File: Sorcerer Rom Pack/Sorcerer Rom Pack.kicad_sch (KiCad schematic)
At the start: 88 parts

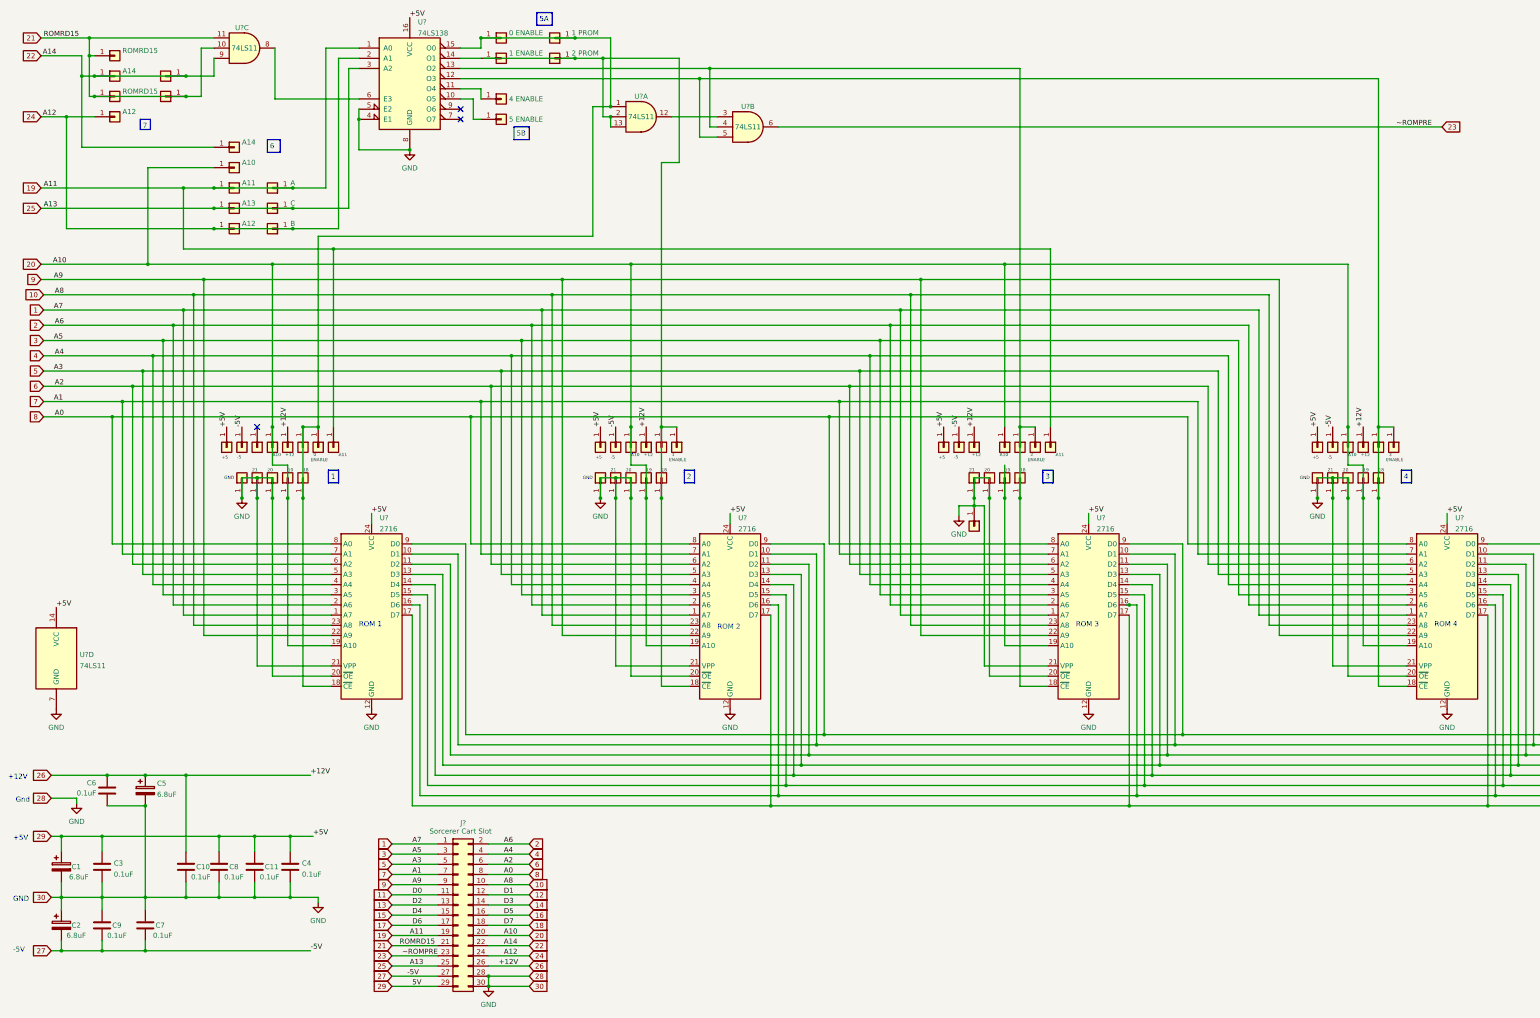
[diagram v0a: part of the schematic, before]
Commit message: added rom pak
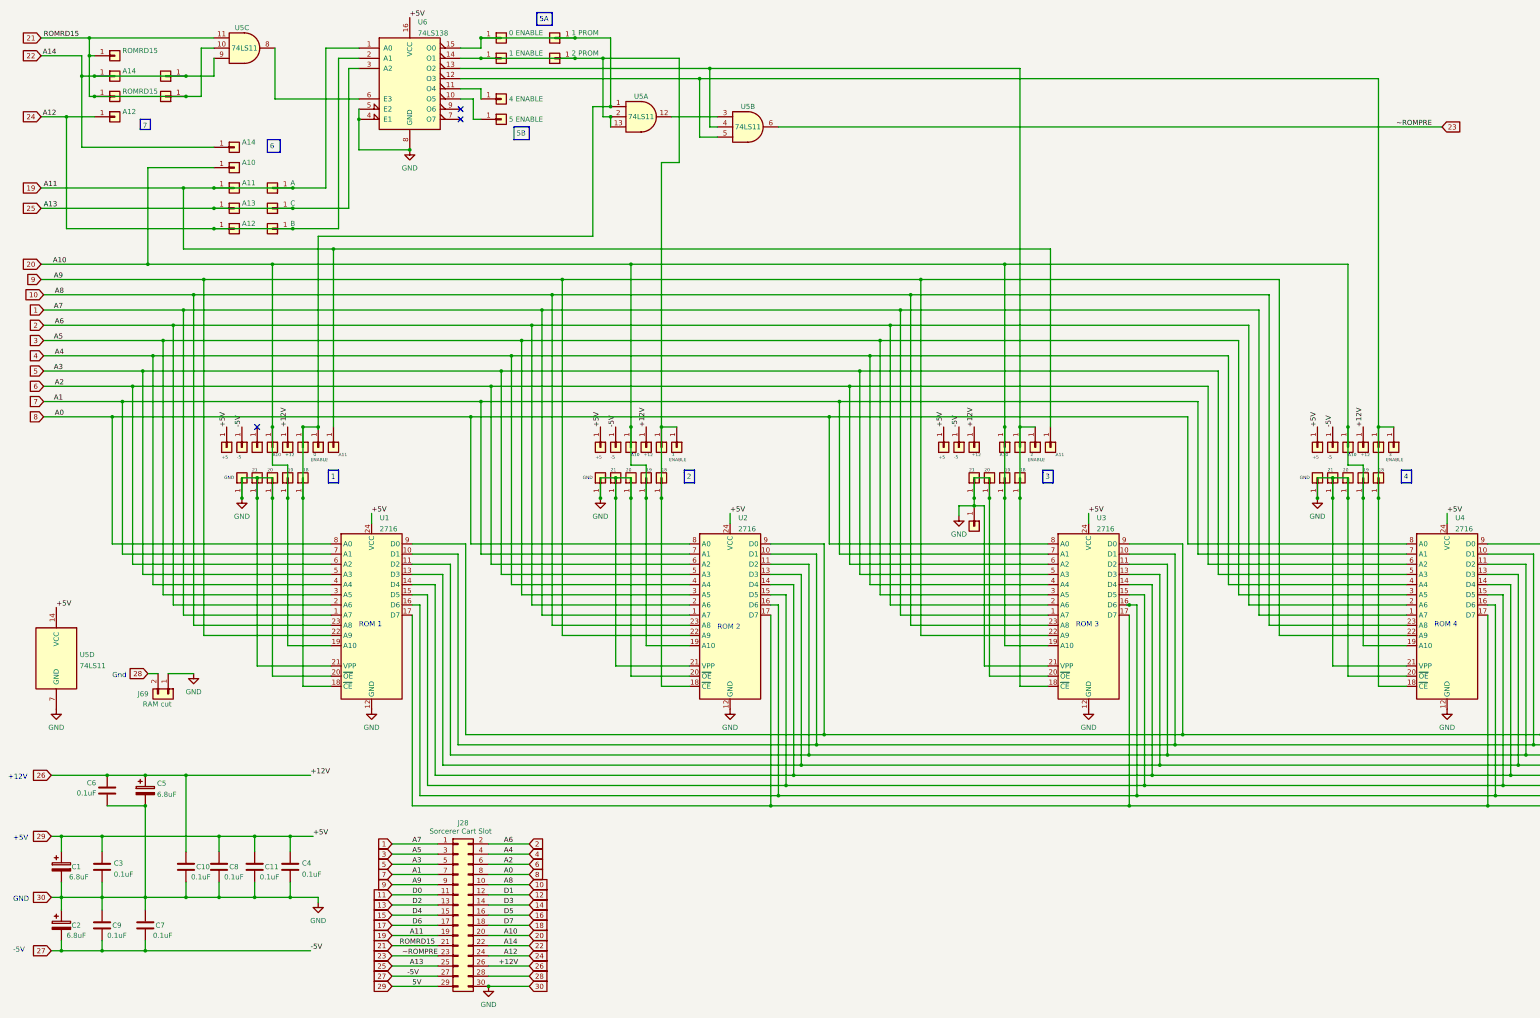
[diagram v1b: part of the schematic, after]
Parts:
- added J69: RAM cut, Jumper:SolderJumper-2_P1.3mm_Open_RoundedPad1.0x1.5mm, symbol Connector_Generic:Conn_01x02
- C1, C2, C5: footprint (none) -> Capacitor_THT:CP_Radial_Tantal_D4.5mm_P5.00mm
- C10, C11, C3, C4, C6, C7, C8, C9: footprint (none) -> Capacitor_THT:C_Disc_D4.3mm_W1.9mm_P5.00mm
- J1, J10, J11, J12, J13, J14, J15, J16, J17, J18, J19, J2, J20, J21, J22, J23, J24, J25, J26, J27, J29, J3, J30, J31, J32, J33, J34, J35, J36, J37, J38, J39, J4, J40, J41, J42, J43, J44, J45, J46, J47, J48, J49, J5, J50, J51, J52, J53, J54, J55, J56, J57, J58, J59, J6, J60, J61, J62, J63, J64, J65, J66, J67, J68, J7, J8, J9: renamed from J?; footprint (none) -> Connector_PinHeader_2.54mm:PinHeader_1x01_P2.54mm_Vertical
- J28: renamed from J?; footprint (none) -> Evan's misc parts:edge mounted 30 pin card edge connector (2x15 pin)
- U5: renamed from U?; footprint (none) -> Package_DIP:DIP-14_W7.62mm
- U6: renamed from U?; footprint (none) -> Package_DIP:DIP-16_W7.62mm
- gave numbers to parts that had none: 4
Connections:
- net 20: now also J53.1 (Pin_1), U3.19 (A10)
- net GND: now also J69.1 (Pin_1); no longer J28.28 (Pin_28)
- net at J30.1 (Pin_1), U6.14 (O1): now also J34.1 (Pin_1), J43.1 (Pin_1), J44.1 (Pin_1), J45.1 (Pin_1), U2.18 (~{CE}), U5.13, U5.2
- new net 28: J28.28 (Pin_28), J69.2 (Pin_2)

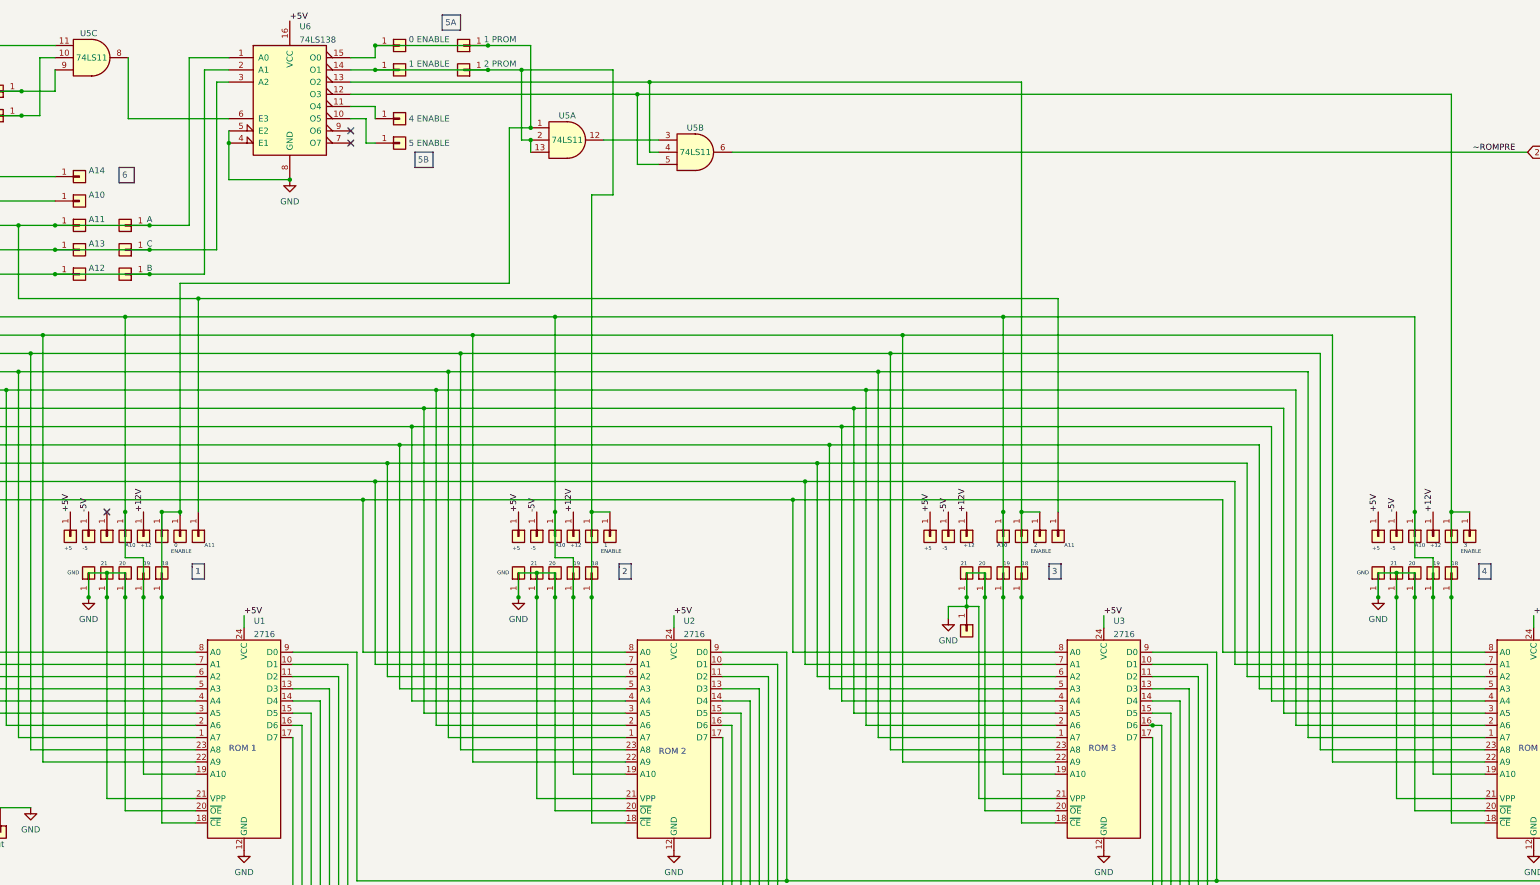
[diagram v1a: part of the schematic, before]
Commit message: many tweaks and experimental silk
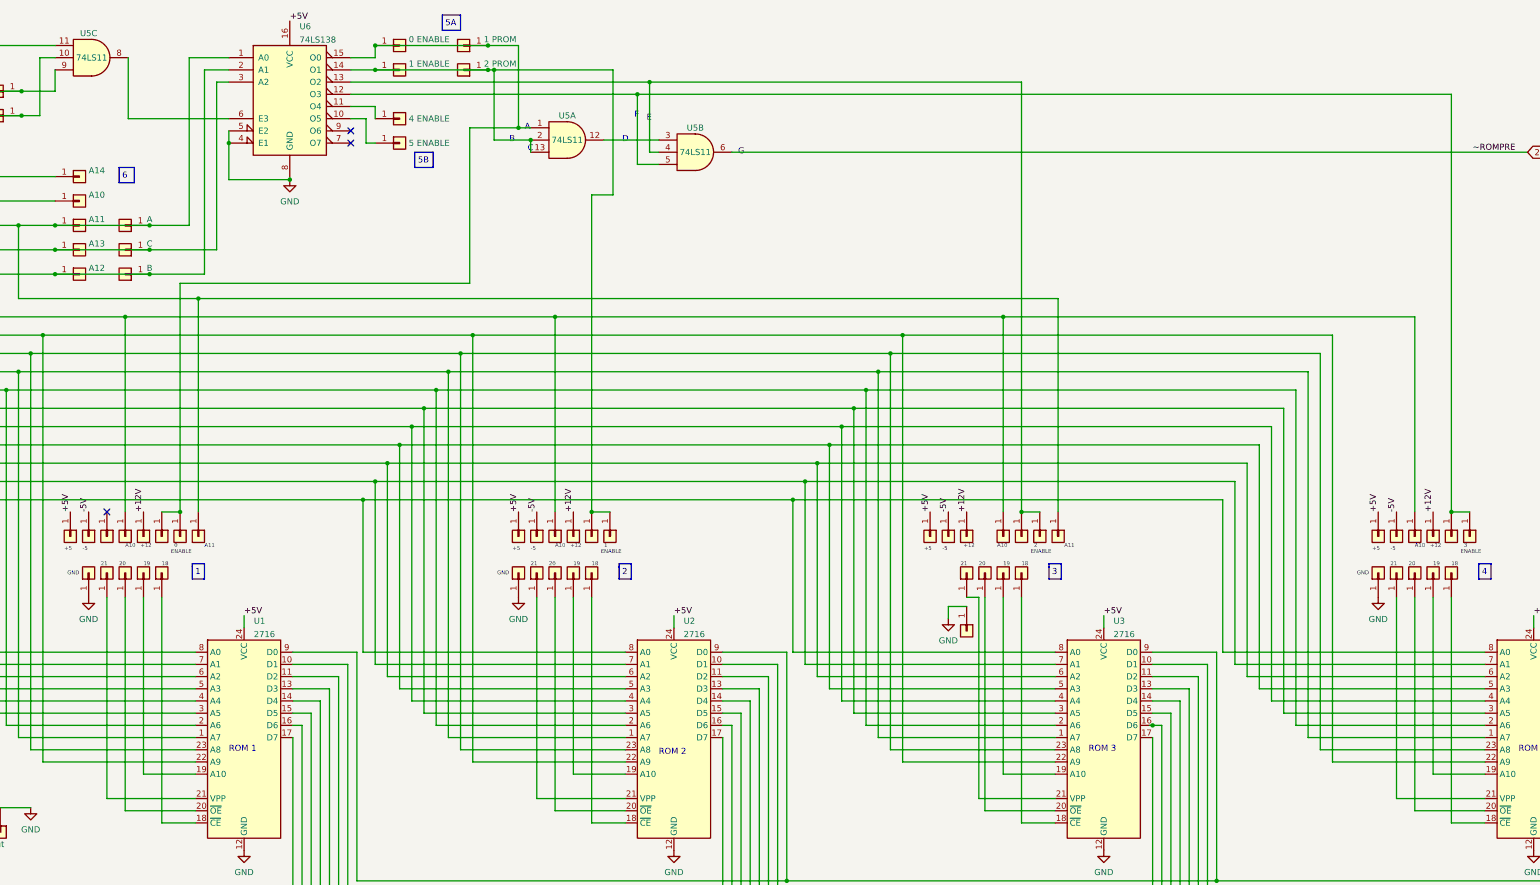
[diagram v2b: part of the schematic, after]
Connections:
- net 20: no longer J23.1 (Pin_1), J42.1 (Pin_1), J53.1 (Pin_1), J65.1 (Pin_1), U1.19 (A10), U2.19 (A10), U3.19 (A10), U4.19 (A10)
- net GND: no longer J16.1 (Pin_1), J21.1 (Pin_1), J38.1 (Pin_1), J40.1 (Pin_1), J49.1 (Pin_1), J51.1 (Pin_1), J61.1 (Pin_1), J63.1 (Pin_1), U1.20 (~{OE}), U1.21 (VPP), U2.20 (~{OE}), U2.21 (VPP), U3.20 (~{OE}), U3.21 (VPP), U4.20 (~{OE}), U4.21 (VPP)
- net at J54.1 (Pin_1), J56.1 (Pin_1), U5.4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: no longer J55.1 (Pin_1), U3.18 (~{CE})
- net at J66.1 (Pin_1), J68.1 (Pin_1), U5.5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: no longer J67.1 (Pin_1), U4.18 (~{CE})
- net at J24.1 (Pin_1), J26.1 (Pin_1), J29.1 (Pin_1)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: no longer J25.1 (Pin_1), U1.18 (~{CE})
- net at J30.1 (Pin_1), J34.1 (Pin_1), J43.1 (Pin_1)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: no longer J44.1 (Pin_1), U2.18 (~{CE})
- new net: J67.1 (Pin_1), U4.18 (~{CE})
- new net: J65.1 (Pin_1), U4.19 (A10)
- new net: J63.1 (Pin_1), U4.20 (~{OE})
- new net: J61.1 (Pin_1), U4.21 (VPP)
- new net: J25.1 (Pin_1), U1.18 (~{CE})
- new net: J23.1 (Pin_1), U1.19 (A10)
- new net: J21.1 (Pin_1), U1.20 (~{OE})
- new net: J16.1 (Pin_1), U1.21 (VPP)
- new net: J53.1 (Pin_1), U3.19 (A10)
- new net: J44.1 (Pin_1), U2.18 (~{CE})
- new net: J42.1 (Pin_1), U2.19 (A10)
- new net: J40.1 (Pin_1), U2.20 (~{OE})
- new net: J38.1 (Pin_1), U2.21 (VPP)
- new net: J55.1 (Pin_1), U3.18 (~{CE})
- new net: J51.1 (Pin_1), U3.20 (~{OE})
- new net: J49.1 (Pin_1), U3.21 (VPP)
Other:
- note added: "A"
- note added: "B"
- note added: "C"
- note added: "D"
- note added: "E"
- note added: "F"
- note added: "G"

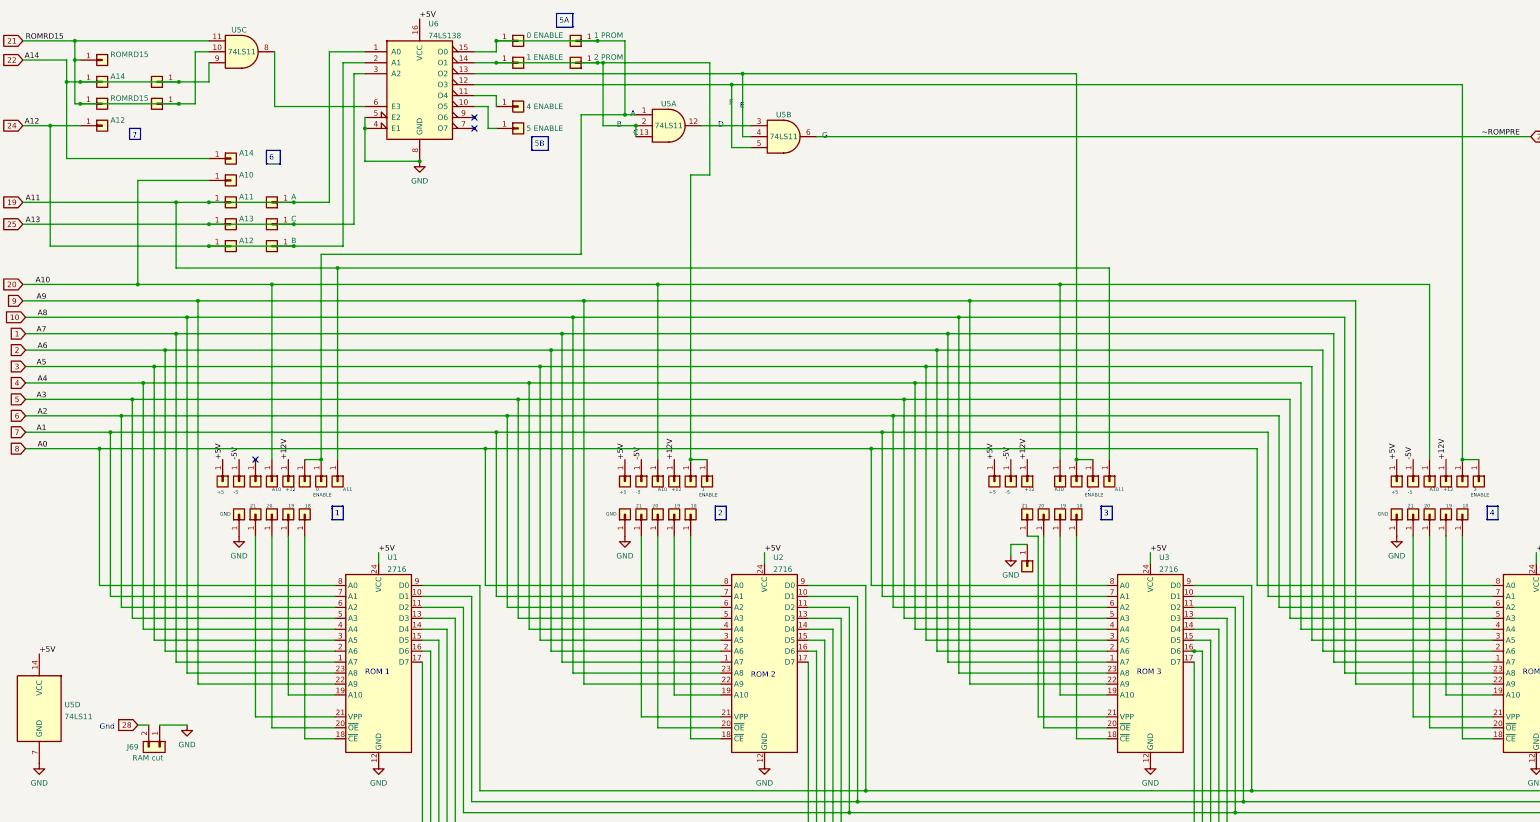
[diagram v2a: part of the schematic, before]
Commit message: removed temp files, added gitignore, fixed silk on rom pac board
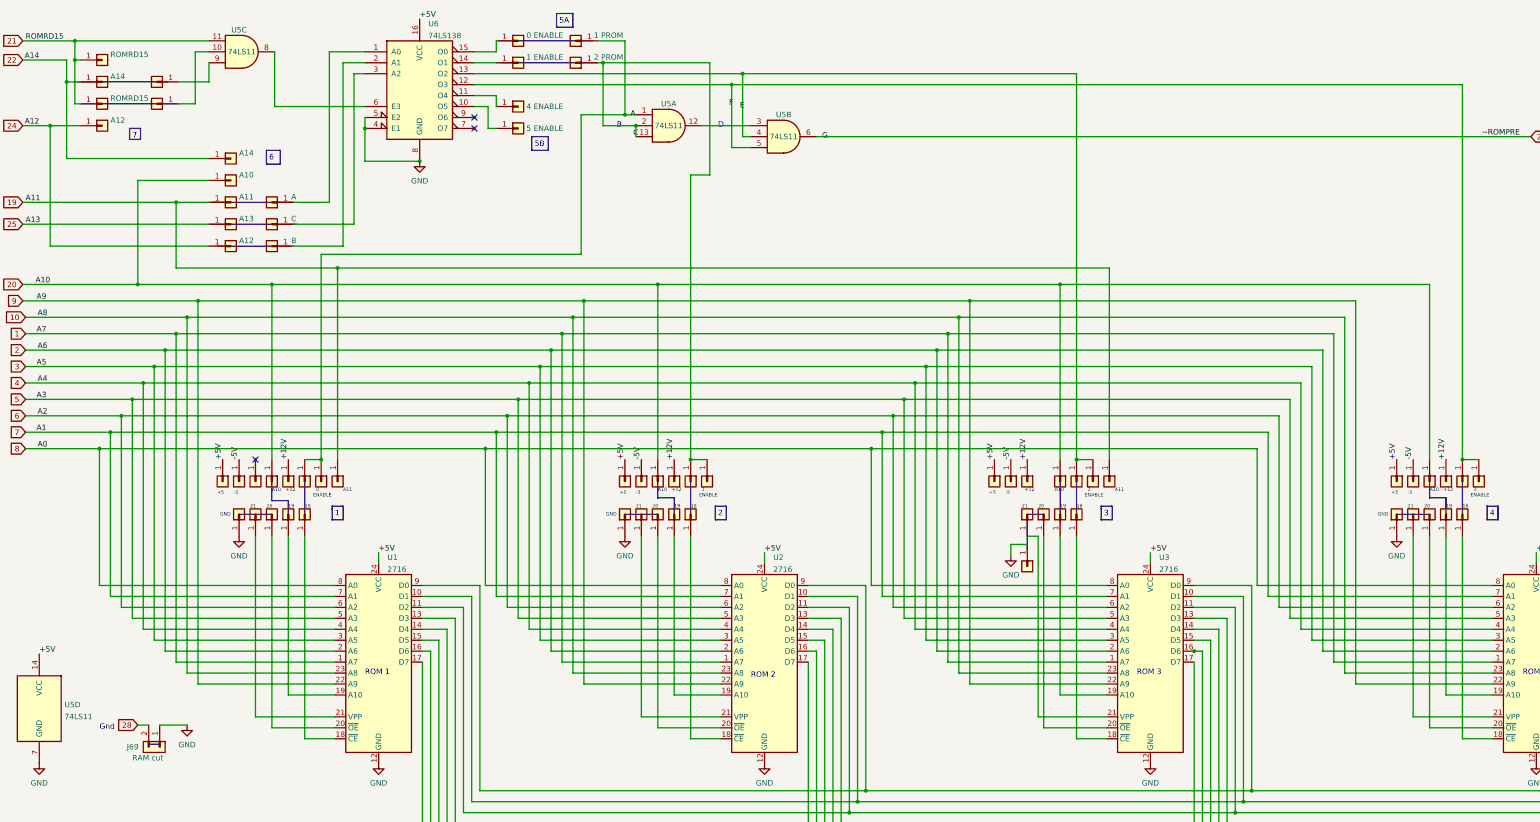
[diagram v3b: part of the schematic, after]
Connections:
- net 19: no longer J17.1 (Pin_1), U6.1 (A0)
- net 21: no longer J6.1 (Pin_1), U5.10
- net 22: no longer J5.1 (Pin_1), U5.9
- net 24: no longer J19.1 (Pin_1), U6.2 (A1)
- net 25: no longer J18.1 (Pin_1), U6.3 (A2)
- net at J34.1 (Pin_1), J43.1 (Pin_1), J45.1 (Pin_1)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: no longer J30.1 (Pin_1), U6.14 (O1)
- net at J24.1 (Pin_1), J26.1 (Pin_1), J33.1 (Pin_1)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: no longer J29.1 (Pin_1), U6.15 (O0)
- new net: J30.1 (Pin_1), U6.14 (O1)
- new net: J29.1 (Pin_1), U6.15 (O0)
- new net: J19.1 (Pin_1), U6.2 (A1)
- new net: J18.1 (Pin_1), U6.3 (A2)
- new net: J6.1 (Pin_1), U5.10
- new net: J5.1 (Pin_1), U5.9
- new net: J17.1 (Pin_1), U6.1 (A0)
